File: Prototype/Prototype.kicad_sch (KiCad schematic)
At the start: 16 parts, among them J1 Conn_01x07, J2 Conn_01x05, J3 Conn_01x01, J4 Conn_01x03, SW1 SW_Push, SW2 SW_Push, SW3 SW_Push, SW4 SW_Push

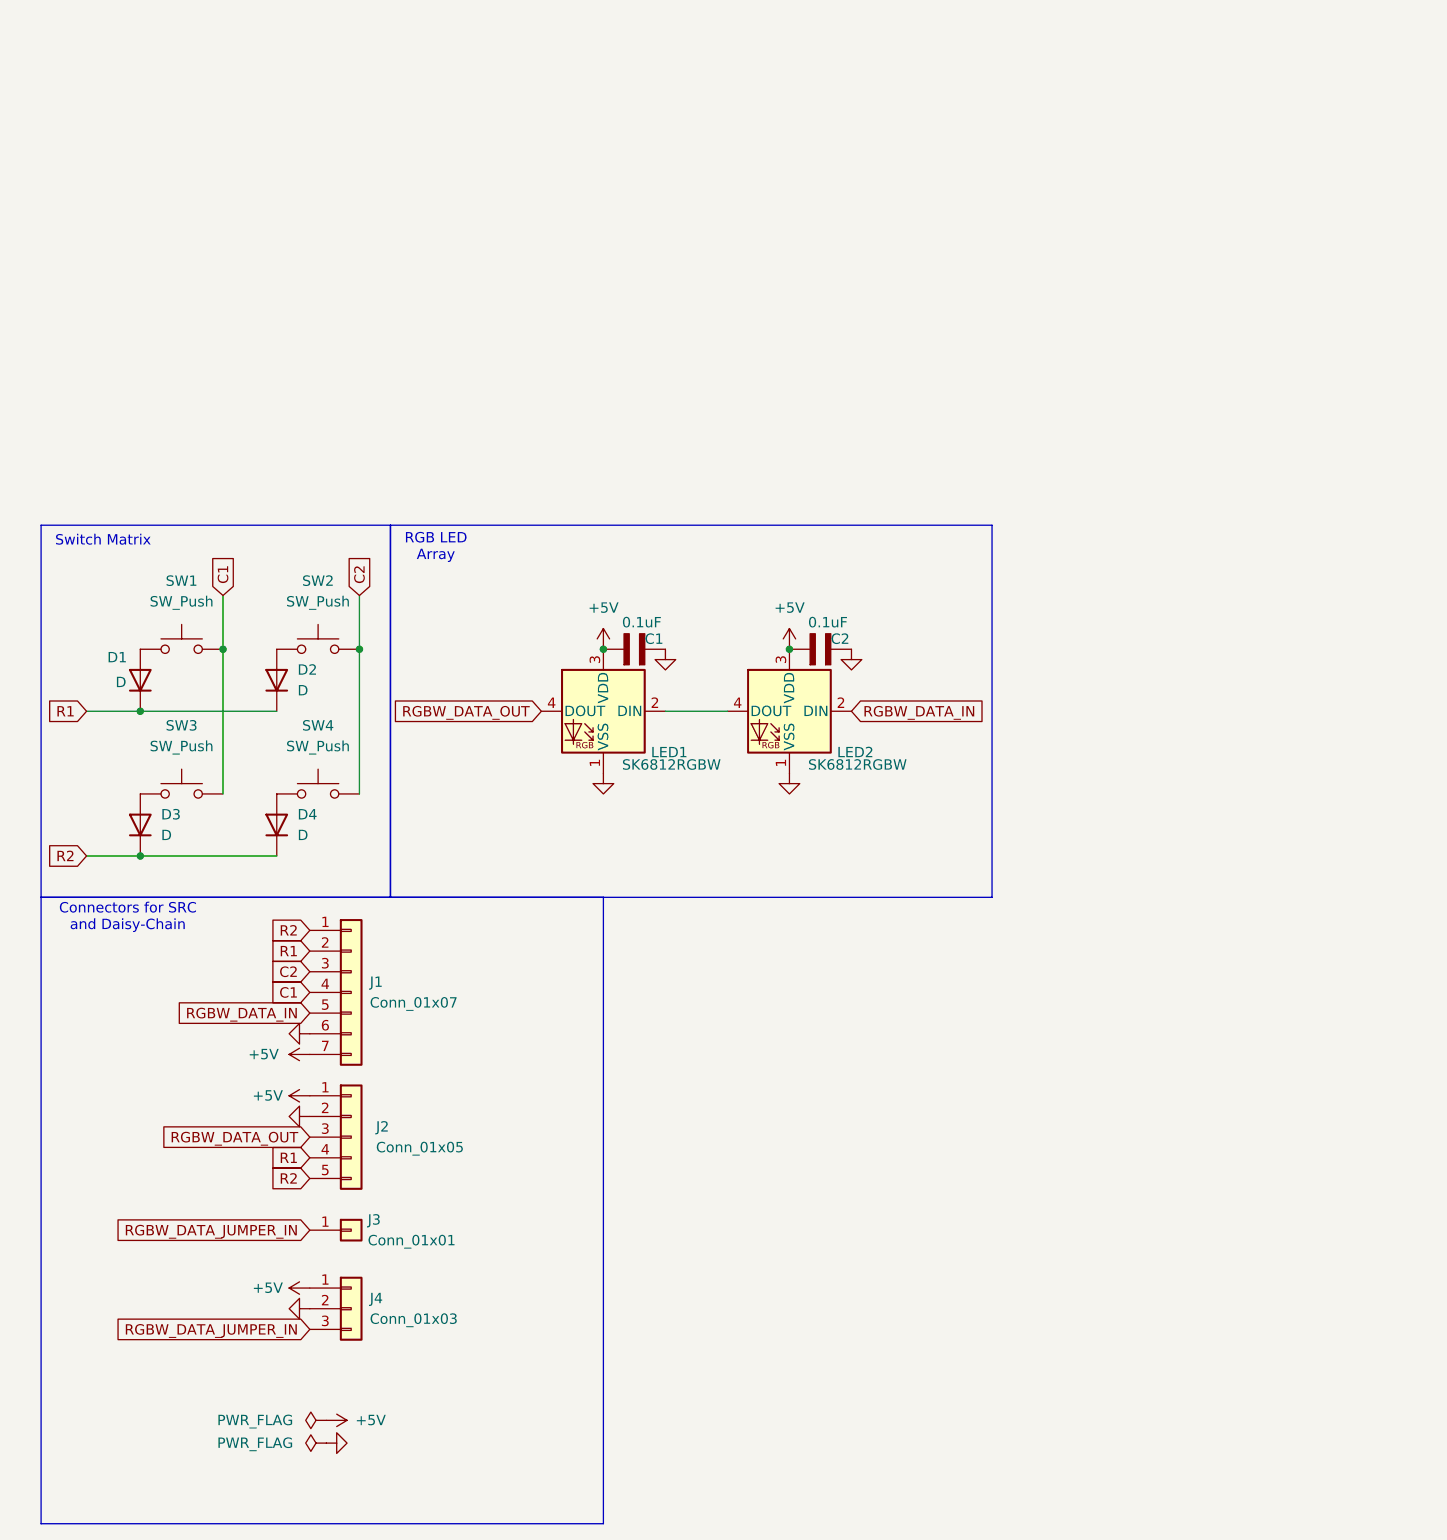
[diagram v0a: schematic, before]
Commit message: work on v0.3 of prototype board, new mounting holes/trace runs
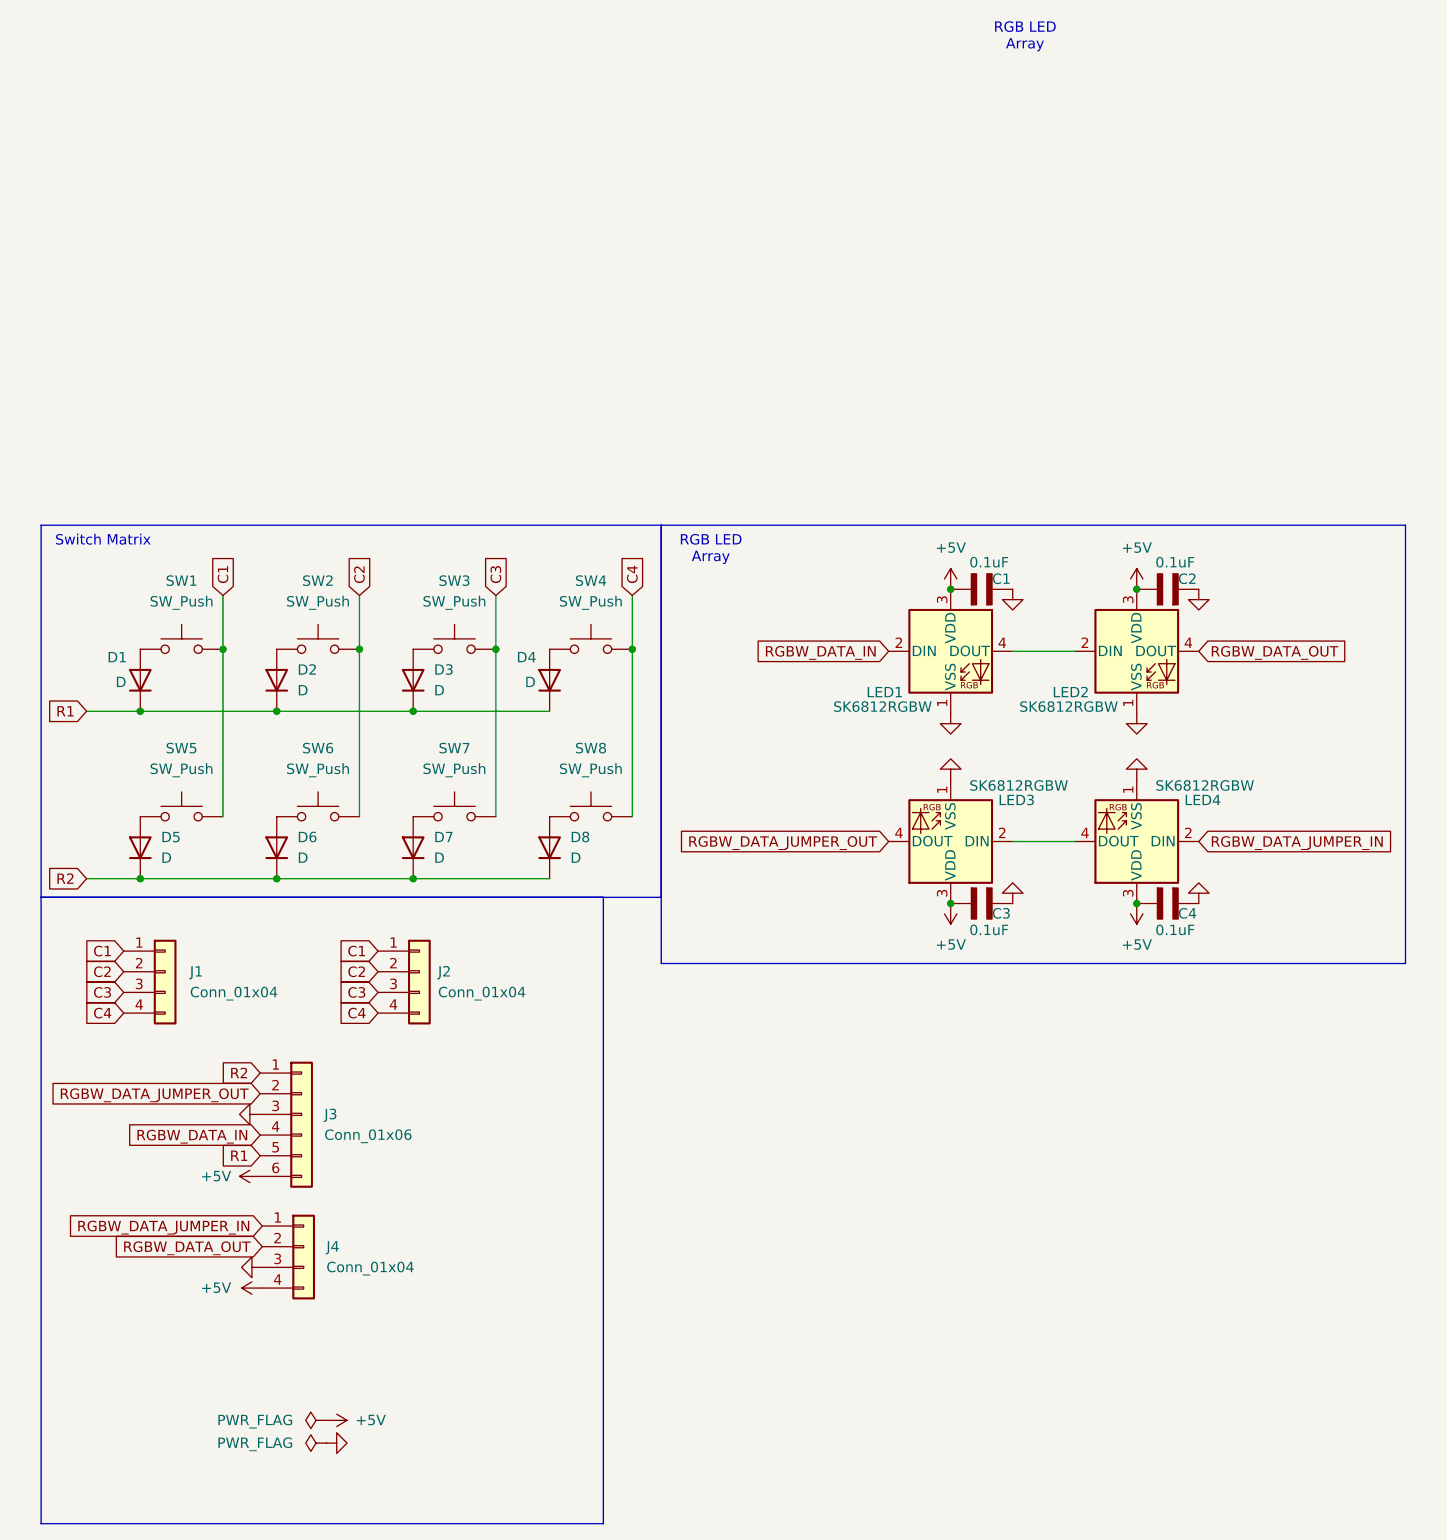
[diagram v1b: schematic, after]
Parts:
- removed J1: Conn_01x07, Connector_PinSocket_2.54mm:PinSocket_1x07_P2.54mm_Horizontal, symbol Connector_Generic:Conn_01x07
- removed J2: Conn_01x05, Connector_PinSocket_2.54mm:PinSocket_1x05_P2.54mm_Horizontal, symbol Connector_Generic:Conn_01x05
- removed J3: Conn_01x01, Connector_PinSocket_2.54mm:PinSocket_1x01_P2.54mm_Horizontal, symbol Connector_Generic:Conn_01x01
- removed J4: Conn_01x03, Connector_PinSocket_2.54mm:PinSocket_1x03_P2.54mm_Vertical, symbol Connector_Generic:Conn_01x03
- added C3, C4: 0.1uF, Capacitor_SMD:C_0402_1005Metric, symbol BOM:C0603T104K8RAC7867
- added D5, D6, D7, D8: D, Diode_SMD:D_SOD-323, symbol Device:D
- added J1, J2, J4: Conn_01x04, Connector_PinSocket_2.00mm:PinSocket_1x04_P2.00mm_Vertical, symbol Connector_Generic:Conn_01x04
- added J3: Conn_01x06, Connector_PinSocket_2.00mm:PinSocket_1x06_P2.00mm_Horizontal, symbol Connector_Generic:Conn_01x06
- added LED3, LED4: SK6812RGBW, BOM:LED_SK6812_PLCC4_5.0x5.0mm_P1.6mm, symbol BOM:SK6812RGBW-WS
- added SW5, SW6, SW7, SW8: SW_Push, ScottoKeebs_Hotswap:Hotswap_MX_1.00u, symbol Switch:SW_Push
- C1, C2: footprint BOM:CAPC1608X87N -> Capacitor_SMD:C_0402_1005Metric; jclpcb.com (none) -> C1525
- D1, D2, D3, D4: footprint BOM:CR_48W-E3-08_VIS -> Diode_SMD:D_SOD-323; jclpcb.com (none) -> C2128
- LED1, LED2: jclpcb.com (none) -> C5378724
- SW1, SW2, SW3, SW4: jclpcb.com (none) -> C41430893
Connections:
- net +5V: now also C3.1, C4.1, J3.6 (Pin_6), J4.4 (Pin_4), LED3.3 (VDD), LED4.3 (VDD)
- net C1: now also J1.1 (Pin_1), J2.1 (Pin_1), SW5.2; no longer SW3.2
- net C2: now also J1.2 (Pin_2), J2.2 (Pin_2), SW6.2; no longer SW4.2
- net GND: now also C3.2, C4.2, J3.3 (Pin_3), J4.3 (Pin_3), LED3.1 (VSS), LED4.1 (VSS)
- net R1: now also D3.1 (K), D4.1 (K), J3.5 (Pin_5)
- net R2: now also D5.1 (K), D6.1 (K), D7.1 (K), D8.1 (K), J3.1 (Pin_1); no longer D3.1 (K), D4.1 (K)
- net RGBW_DATA_IN: now also LED1.2 (DIN), J3.4 (Pin_4); no longer LED2.2 (DIN)
- net RGBW_DATA_JUMPER_IN: now also J4.1 (Pin_1), LED4.2 (DIN)
- net RGBW_DATA_OUT: now also LED2.4 (DOUT), J4.2 (Pin_2); no longer LED1.4 (DOUT)
- new net: D6.2 (A), SW6.1
- new net: LED1.4 (DOUT), LED2.2 (DIN)
- new net: D7.2 (A), SW7.1
- new net: D5.2 (A), SW5.1
- new net: LED3.2 (DIN), LED4.4 (DOUT)
- new net: D8.2 (A), SW8.1
- new net C3: J1.3 (Pin_3), J2.3 (Pin_3), SW3.2, SW7.2
- new net C4: J1.4 (Pin_4), J2.4 (Pin_4), SW4.2, SW8.2
- new net RGBW_DATA_JUMPER_OUT: J3.2 (Pin_2), LED3.4 (DOUT)
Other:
- note removed: "Connectors for SRC and Daisy-Chain"
- moved on the sheet: C1, C2, LED1, LED2
